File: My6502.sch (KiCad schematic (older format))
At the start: 27 parts, among them J1 IRQ_SEL, J2 CLK Jumper, J3 Barrel_Jack_Switch, J4 Expansion Port, J5 IRQ_Pullup, SW1 SW_Push_Dual, U1 28C256, U2 WD65C02, U3 CY62256-70PC, U4 74HCT00, U5 74HCT02, U6 DS1813-10, U7 74LS21, X1 CXO_DIP14

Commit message: pcb with a 10x10 board`
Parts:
- added C7: 0.1uF, Capacitor_THT:C_Disc_D4.3mm_W1.9mm_P5.00mm, symbol Device:C
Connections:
- net +5V: now also C7.1
- net GND: now also C7.2
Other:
- moved on the sheet: C6
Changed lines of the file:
@@
 L Device:C C6
 U 1 1 6163A5A8
-P 8900 4800
-F 0 "C6" H 9015 4846 50  0000 L CNN
-F 1 "0.1uF" H 9015 4755 50  0000 L CNN
-F 2 "Capacitor_THT:C_Disc_D4.3mm_W1.9mm_P5.00mm" H 8938 4650 50  0001 C CNN
-F 3 "~" H 8900 4800 50  0001 C CNN
-	1    8900 4800
+P 9050 4800
+F 0 "C6" H 9165 4846 50  0000 L CNN
+F 1 "0.1uF" H 9165 4755 50  0000 L CNN
+F 2 "Capacitor_THT:C_Disc_D4.3mm_W1.9mm_P5.00mm" H 9088 4650 50  0001 C CNN
+F 3 "~" H 9050 4800 50  0001 C CNN
+	1    9050 4800
 	1    0    0    -1
 $EndComp
@@
 	8150 5300 7700 5300
 Wire Wire Line
-	8900 4650 8900 4300
+	9050 4650 8900 4300
 Connection ~ 8900 4300
 Wire Wire Line
-	8900 4300 8150 4300
+	8900 4300 8600 4300
 Wire Wire Line
 	8150 4650 8150 4300
@@
 $EndComp
 Wire Wire Line
-	8900 5300 8150 5300
+	8900 5300 8600 5300
 Connection ~ 8900 5300
 Wire Wire Line
-	8900 4950 8900 5300
+	9050 4950 8900 5300
 Wire Wire Line
 	9500 5300 8900 5300
@@
 Wire Wire Line
 	8850 6600 8850 7450
+$Comp
+L Device:C C7
+U 1 1 63306EB2
+P 8600 4800
+F 0 "C7" H 8715 4846 50  0000 L CNN
+F 1 "0.1uF" H 8715 4755 50  0000 L CNN
+F 2 "Capacitor_THT:C_Disc_D4.3mm_W1.9mm_P5.00mm" H 8638 4650 50  0001 C CNN
+F 3 "~" H 8600 4800 50  0001 C CNN
+	1    8600 4800
+	1    0    0    -1
+$EndComp
+Wire Wire Line
+	8600 4650 8600 4300
+Connection ~ 8600 4300
+Wire Wire Line
+	8600 4300 8150 4300
+Wire Wire Line
+	8600 4950 8600 5300
+Connection ~ 8600 5300
+Wire Wire Line
+	8600 5300 8150 5300
 Wire Bus Line
 	4950 2600 4950 3800

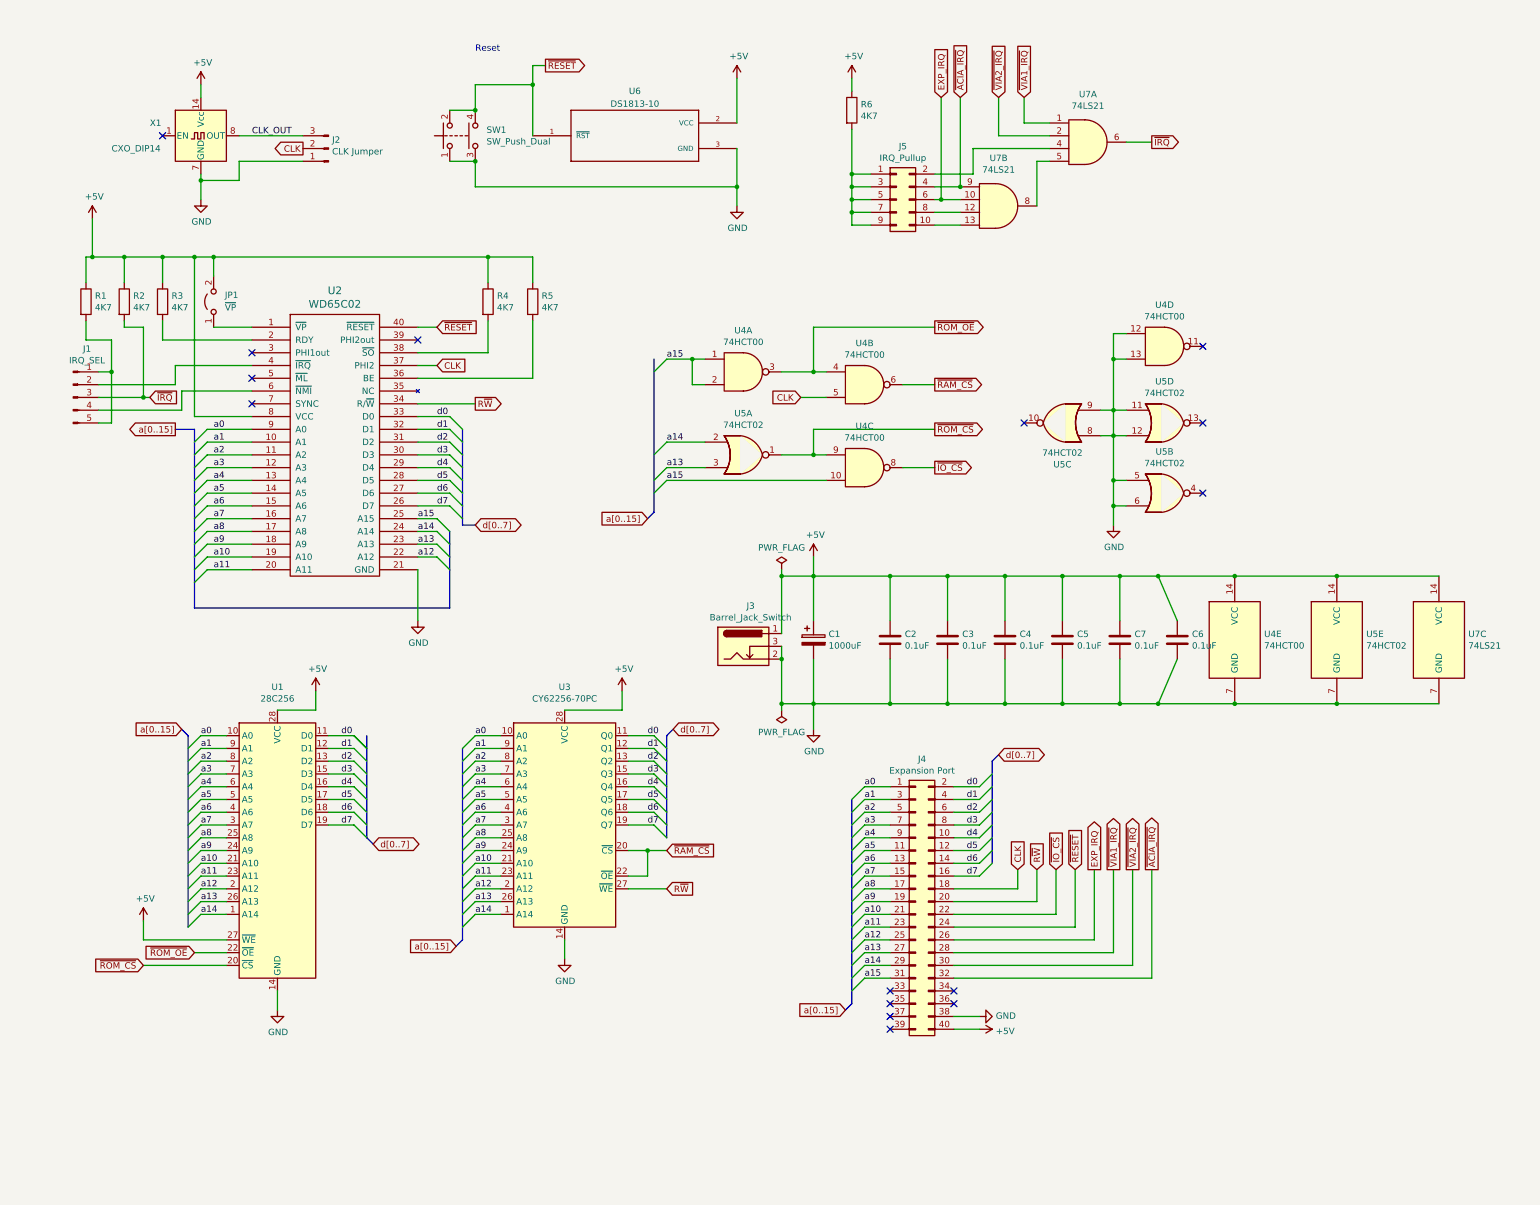
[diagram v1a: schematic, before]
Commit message: Edge board completed and routed
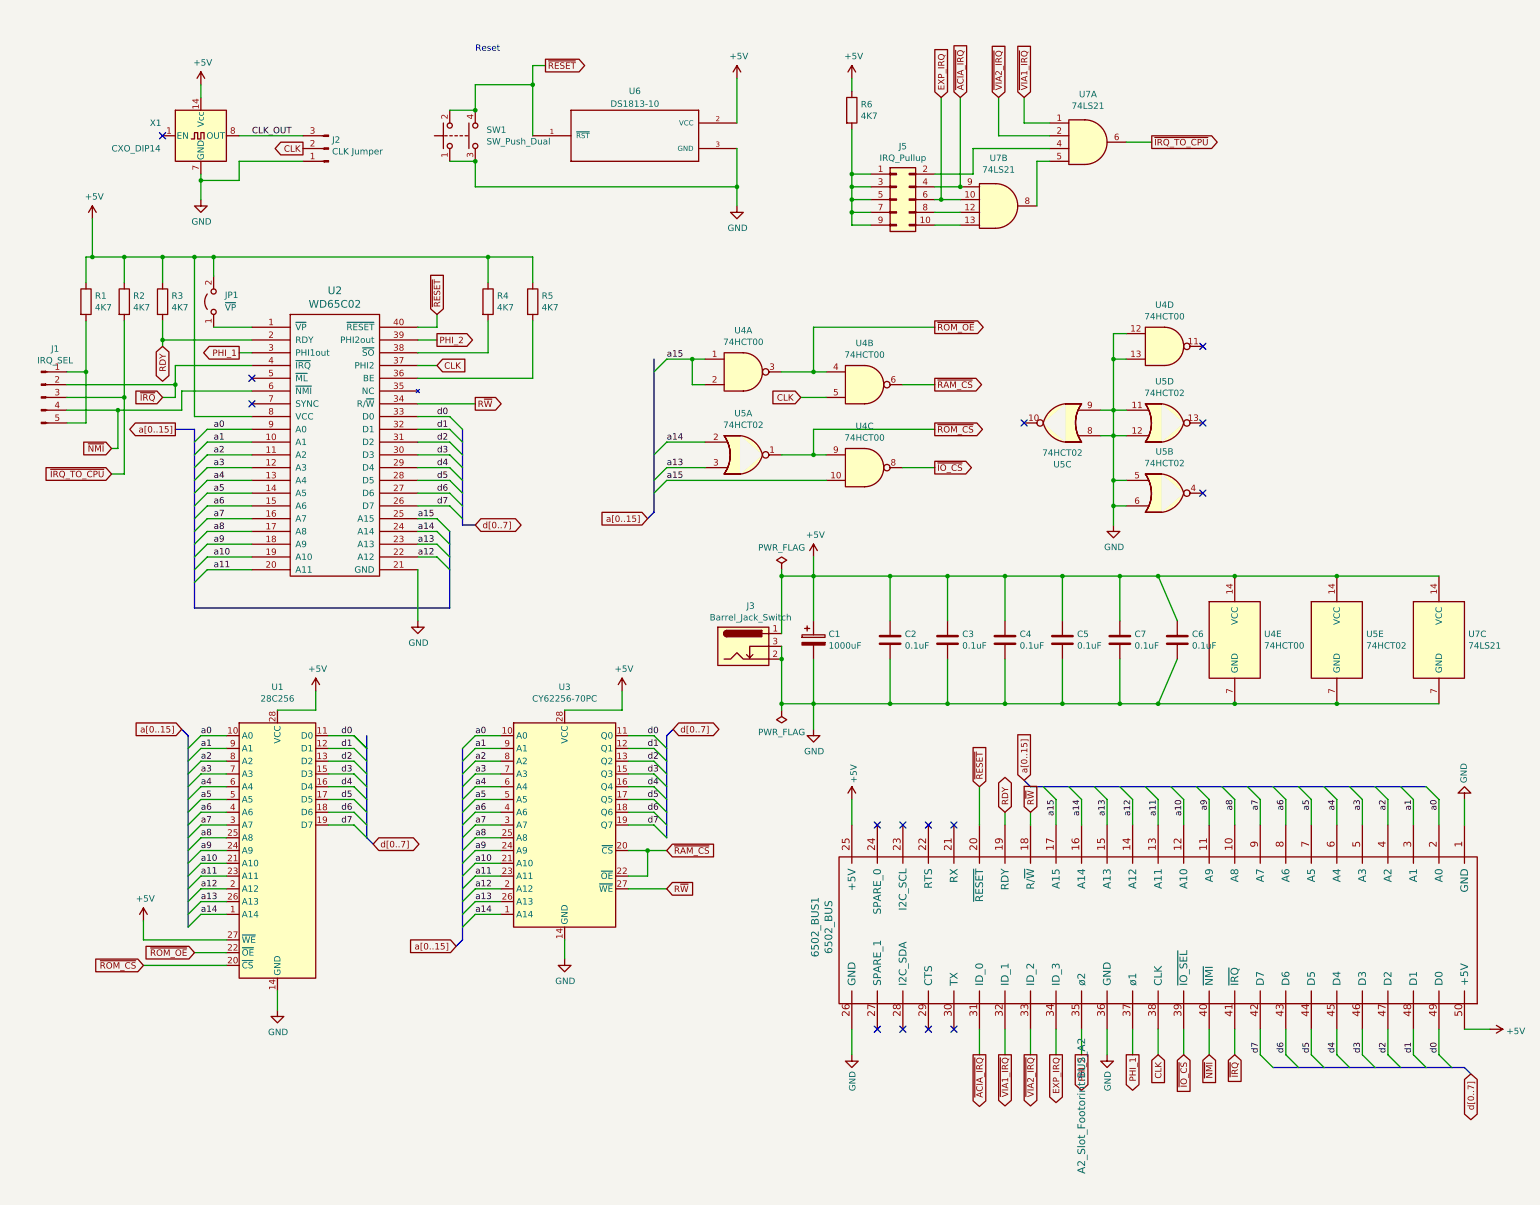
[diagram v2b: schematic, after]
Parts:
- removed J4: Expansion Port, Connector_PinSocket_2.54mm:PinSocket_2x20_P2.54mm_Vertical, symbol Connector_Generic:Conn_02x20_Odd_Even
- added 6502_BUS1: 6502_BUS, A2_Slot_Footorint:BUS_A2, symbol My6502:6502_BUS
- U2: footprint Package_DIP:DIP-40_W25.4mm_Socket_LongPads -> Package_DIP:DIP-40_W15.24mm_Socket_LongPads
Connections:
- net +5V: now also 6502_BUS1.25 (+5V), 6502_BUS1.50 (+5V)
- net CLK: now also 6502_BUS1.38 (CLK)
- net EXP_IRQ: now also 6502_BUS1.34 (ID_3)
- net GND: now also 6502_BUS1.1 (GND), 6502_BUS1.26 (GND), 6502_BUS1.36 (GND)
- net R~W: now also 6502_BUS1.18 (R/~W)
- net a0: now also 6502_BUS1.2 (A0)
- net a1: now also 6502_BUS1.3 (A1)
- net a10: now also 6502_BUS1.12 (A10)
- net a11: now also 6502_BUS1.13 (A11)
- net a12: now also 6502_BUS1.14 (A12)
- net a13: now also 6502_BUS1.15 (A13)
- net a14: now also 6502_BUS1.16 (A14)
- net a15: now also 6502_BUS1.17 (A15)
- net a2: now also 6502_BUS1.4 (A2)
- net a3: now also 6502_BUS1.5 (A3)
- net a4: now also 6502_BUS1.6 (A4)
- net a5: now also 6502_BUS1.7 (A5)
- net a6: now also 6502_BUS1.8 (A6)
- net a7: now also 6502_BUS1.9 (A7)
- net a8: now also 6502_BUS1.10 (A8)
- net a9: now also 6502_BUS1.11 (A9)
- net d0: now also 6502_BUS1.49 (D0)
- net d1: now also 6502_BUS1.48 (D1)
- net d2: now also 6502_BUS1.47 (D2)
- net d3: now also 6502_BUS1.46 (D3)
- net d4: now also 6502_BUS1.45 (D4)
- net d5: now also 6502_BUS1.44 (D5)
- net d6: now also 6502_BUS1.43 (D6)
- net d7: now also 6502_BUS1.42 (D7)
- net ~ACIA_IRQ: now also 6502_BUS1.31 (ID_0)
- net ~IO_CS: now also 6502_BUS1.39 (~IO_SEL)
- net ~IRQ: now also J1.2 (Pin_2), U2.4 (~IRQ), 6502_BUS1.41 (~IRQ); no longer J1.3 (Pin_3), R2.2, U7.6
- net ~RESET: now also 6502_BUS1.20 (~RESET)
- net ~VIA1_IRQ: now also 6502_BUS1.32 (ID_1)
- net ~VIA2_IRQ: now also 6502_BUS1.33 (ID_2)
- net RDY: now reaches R3.2, U2.2 (RDY)
- net RDY: now also 6502_BUS1.19 (RDY)
- net PHI_1: now reaches U2.3 (PHI1out)
- net PHI_1: now also 6502_BUS1.37 (ø1)
- net PHI_2: now reaches U2.39 (PHI2out)
- net PHI_2: now also 6502_BUS1.35 (ø2)
- net ~NMI: now reaches J1.4 (Pin_4), U2.6 (~NMI)
- net ~NMI: now also 6502_BUS1.40 (~NMI)
- new net ~IRQ_TO_CPU: J1.3 (Pin_3), R2.2, U7.6
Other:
- moved on the sheet: J1

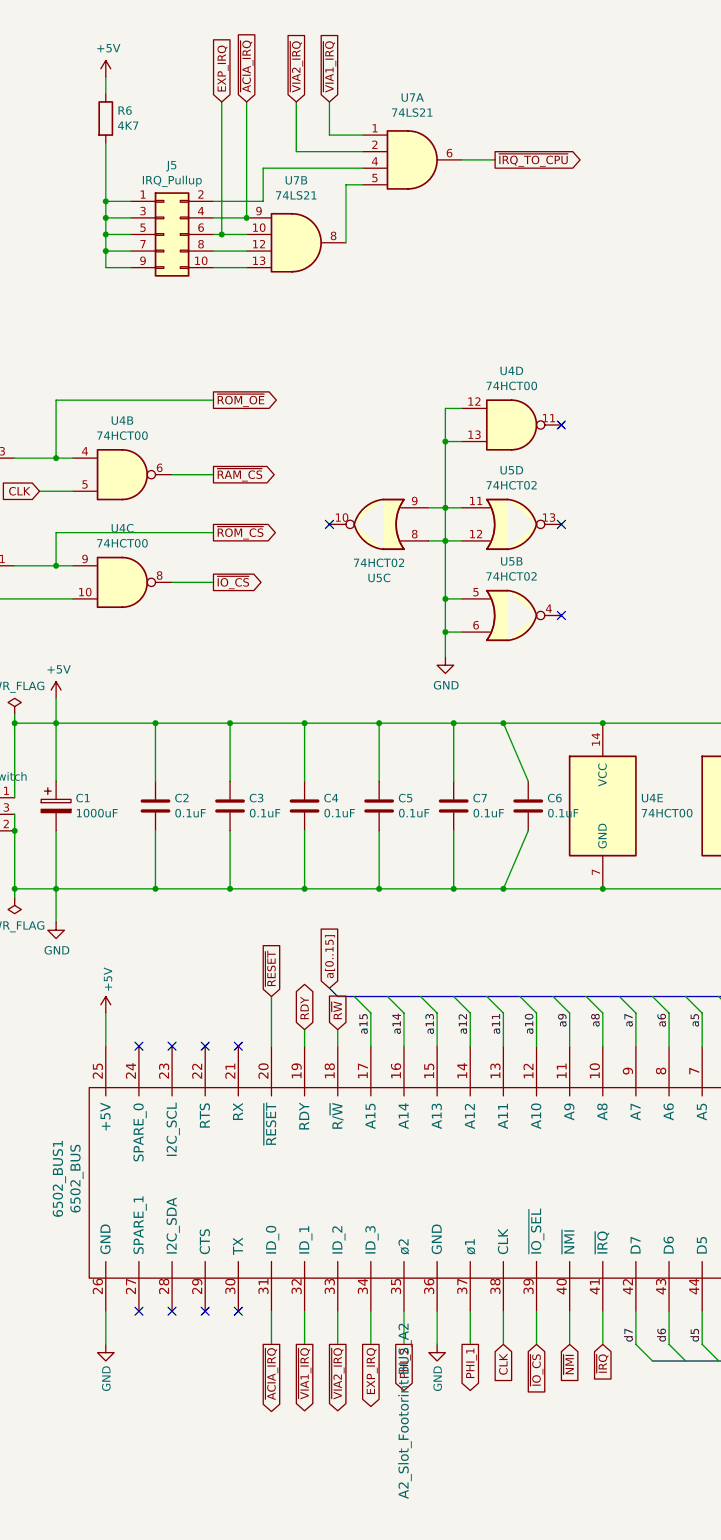
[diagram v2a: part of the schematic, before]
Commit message: moving to a backplane
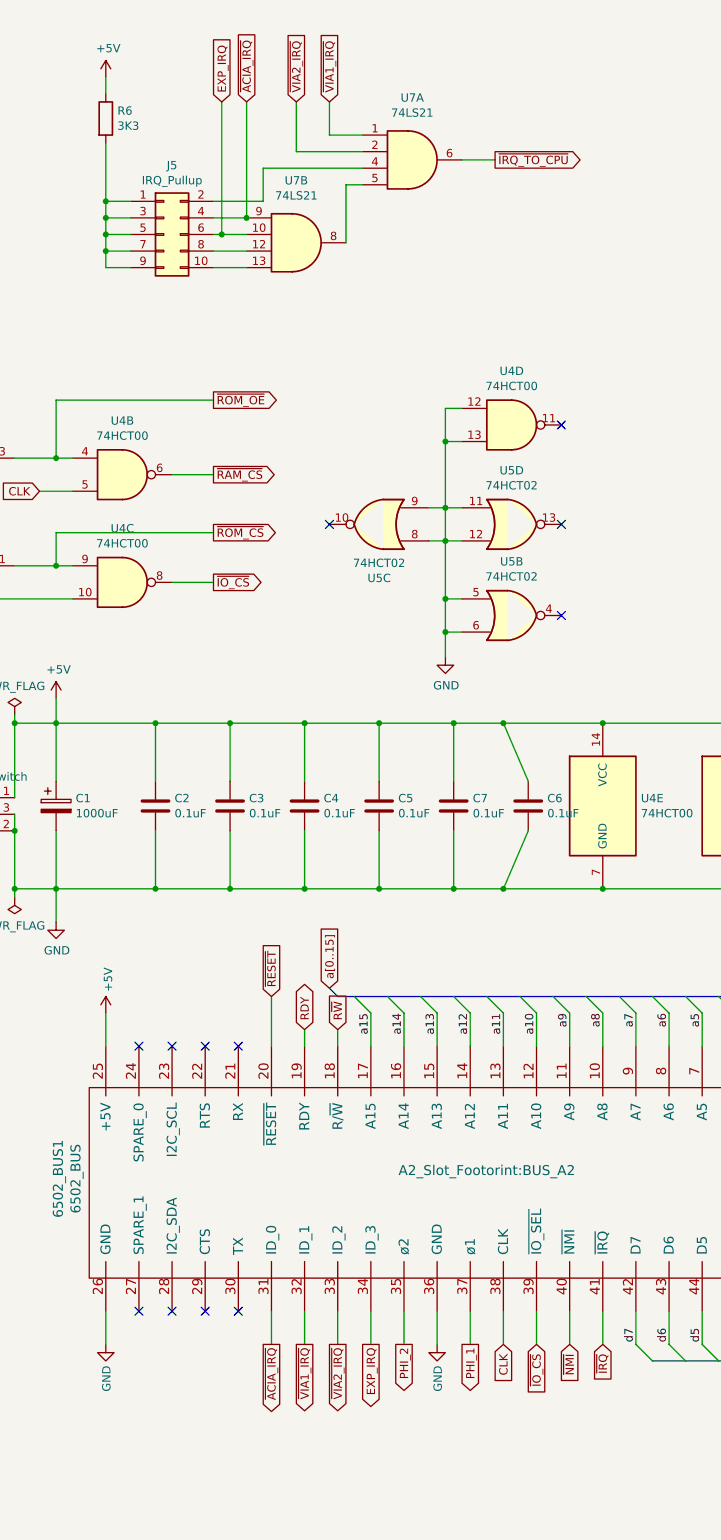
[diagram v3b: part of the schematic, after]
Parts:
- R6: value 4K7 -> 3K3
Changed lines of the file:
@@
 	800  2900 350  2900
-$Comp
-L DS1813-10:DS1813-10 U6
-U 1 1 61278A1B
-P 4800 850
-F 0 "U6" H 4800 1200 50  0000 C CNN
-F 1 "DS1813-10" H 4800 1100 50  0000 C CNN
-F 2 "Package_TO_SOT_THT:TO-92" H 4800 850 50  0001 L BNN
-F 3 "" H 4800 850 50  0001 L BNN
-F 4 "MAXIM" H 4800 850 50  0001 L BNN "VENDOR"
-F 5 "ds181315+" H 4800 850 50  0001 L BNN "MANUFACTURER_PART_NUMBER"
-	1    4800 850
-	1    0    0    -1
-$EndComp
-Text Notes 3550 200  0    50   ~ 0
-Reset
-$Comp
-L power:+5V #PWR010
-U 1 1 61279C80
-P 5600 400
-F 0 "#PWR010" H 5600 250 50  0001 C CNN
-F 1 "+5V" H 5615 573 50  0000 C CNN
-F 2 "" H 5600 400 50  0001 C CNN
-F 3 "" H 5600 400 50  0001 C CNN
-	1    5600 400
-	1    0    0    -1
-$EndComp
-$Comp
-L power:GND #PWR011
-U 1 1 6127B348
-P 5600 1400
-F 0 "#PWR011" H 5600 1150 50  0001 C CNN
-F 1 "GND" H 5605 1227 50  0000 C CNN
-F 2 "" H 5600 1400 50  0001 C CNN
-F 3 "" H 5600 1400 50  0001 C CNN
-	1    5600 1400
-	1    0    0    -1
-$EndComp
-Wire Wire Line
-	3550 1250 5600 1250
-Wire Wire Line
-	5600 1250 5600 1400
-Wire Wire Line
-	5600 950  5600 1250
-Connection ~ 5600 1250
-Wire Wire Line
-	5600 750  5600 400
 $Comp
 L Oscillator:CXO_DIP14 X1
@@
 Wire Wire Line
 	8550 2600 8550 3000
-Wire Wire Line
-	4000 850  4000 450
-Wire Wire Line
-	4000 450  3550 450
-Text GLabel 4100 300  2    50   Output ~ 0
-~RESET
 $Comp
 L Memory_RAM:CY62256-70PC U3
@@
 Wire Wire Line
 	8450 3000 8550 3000
-Connection ~ 3550 650
-Wire Wire Line
-	3550 450  3550 650
-Connection ~ 3550 1050
-Wire Wire Line
-	3550 1250 3550 1050
-Wire Wire Line
-	3350 650  3550 650
-Wire Wire Line
-	3350 1050 3550 1050
-$Comp
-L Switch:SW_Push_Dual SW1
-U 1 1 6127D438
-P 3350 850
-F 0 "SW1" V 3396 562 50  0000 R CNN
-F 1 "SW_Push_Dual" V 3305 562 50  0000 R CNN
-F 2 "Button_Switch_THT:SW_TH_Tactile_Omron_B3F-10xx" H 3350 1050 50  0001 C CNN
-F 3 "~" H 3350 1050 50  0001 C CNN
-	1    3350 850
-	0    -1   -1   0
-$EndComp
-Wire Wire Line
-	4100 300  4000 300
-Wire Wire Line
-	4000 300  4000 450
-Connection ~ 4000 450
 $Comp
 L 74xx:74LS21 U7
@@
 P 6500 650
 F 0 "R6" H 6570 696 50  0000 L CNN
-F 1 "4K7" H 6570 605 50  0000 L CNN
+F 1 "3K3" H 6570 605 50  0000 L CNN
 F 2 "Resistor_THT:R_Axial_DIN0207_L6.3mm_D2.5mm_P10.16mm_Horizontal" V 6430 650 50  0001 L CNN
 F 3 "~" H 6500 650 50  0001 L CNN
@@
 F 0 "6502_BUS1" H 9700 10537 60  0000 C CNN
 F 1 "6502_BUS" H 9700 10431 60  0000 C CNN
-F 2 "A2_Slot_Footorint:BUS_A2" H 8300 8450 60  0000 C CNN
+F 2 "A2_Slot_Footorint:BUS_A2" V 9750 7950 60  0000 C CNN
 F 3 "" H 8300 8450 60  0000 C CNN
 	1    8300 8450
@@
 	8100 8050 8100 7850
 Wire Bus Line
+	9800 8150 11300 8150
+Wire Bus Line
+	7900 5950 11000 5950
+Wire Bus Line
+	1300 5550 1300 7050
+Wire Bus Line
+	3450 5650 3450 7150
+Wire Bus Line
+	5050 5550 5050 6350
+Wire Bus Line
+	2700 5550 2700 6350
+Wire Bus Line
 	4950 2600 4950 3800
 Wire Bus Line
+	1350 3150 1350 4550
+Wire Bus Line
 	3350 3950 3350 4550
 Wire Bus Line
-	9800 8150 11300 8150
-Wire Bus Line
-	5050 5550 5050 6350
-Wire Bus Line
-	2700 5550 2700 6350
-Wire Bus Line
 	3450 3150 3450 3900
-Wire Bus Line
-	1350 3150 1350 4550
-Wire Bus Line
-	3450 5650 3450 7150
-Wire Bus Line
-	1300 5550 1300 7050
-Wire Bus Line
-	7900 5950 11000 5950
+Connection ~ 4000 450
+Wire Wire Line
+	4000 300  4000 450
+Wire Wire Line
+	4100 300  4000 300
+$Comp
+L Switch:SW_Push_Dual SW1
+U 1 1 6127D438
+P 3350 850
+F 0 "SW1" V 3396 562 50  0000 R CNN
+F 1 "SW_Push_Dual" V 3305 562 50  0000 R CNN
+F 2 "Button_Switch_THT:SW_TH_Tactile_Omron_B3F-10xx" H 3350 1050 50  0001 C CNN
+F 3 "~" H 3350 1050 50  0001 C CNN
+	1    3350 850
+	0    -1   -1   0
+$EndComp
+Wire Wire Line
+	3350 1050 3550 1050
+Wire Wire Line
+	3350 650  3550 650
+Wire Wire Line
+	3550 1250 3550 1050
+Connection ~ 3550 1050
+Wire Wire Line
+	3550 450  3550 650
+Connection ~ 3550 650
+Text GLabel 4100 300  2    50   Output ~ 0
+~RESET
+Wire Wire Line
+	4000 450  3550 450
+Wire Wire Line
+	4000 850  4000 450
+Wire Wire Line
+	5600 750  5600 400
+Connection ~ 5600 1250
+Wire Wire Line
+	5600 950  5600 1250
+Wire Wire Line
+	5600 1250 5600 1400
+Wire Wire Line
+	3550 1250 5600 1250
+$Comp
+L power:GND #PWR011
+U 1 1 6127B348
+P 5600 1400
+F 0 "#PWR011" H 5600 1150 50  0001 C CNN
+F 1 "GND" H 5605 1227 50  0000 C CNN
+F 2 "" H 5600 1400 50  0001 C CNN
+F 3 "" H 5600 1400 50  0001 C CNN
+	1    5600 1400
+	1    0    0    -1
+$EndComp
+$Comp
+L power:+5V #PWR010
+U 1 1 61279C80
+P 5600 400
+F 0 "#PWR010" H 5600 250 50  0001 C CNN
+F 1 "+5V" H 5615 573 50  0000 C CNN
+F 2 "" H 5600 400 50  0001 C CNN
+F 3 "" H 5600 400 50  0001 C CNN
+	1    5600 400
+	1    0    0    -1
+$EndComp
+Text Notes 3550 200  0    50   ~ 0
+Reset
+$Comp
+L DS1813-10:DS1813-10 U6
+U 1 1 61278A1B
+P 4800 850
+F 0 "U6" H 4800 1200 50  0000 C CNN
+F 1 "DS1813-10" H 4800 1100 50  0000 C CNN
+F 2 "Package_TO_SOT_THT:TO-92" H 4800 850 50  0001 L BNN
+F 3 "" H 4800 850 50  0001 L BNN
+F 4 "MAXIM" H 4800 850 50  0001 L BNN "VENDOR"
+F 5 "ds181315+" H 4800 850 50  0001 L BNN "MANUFACTURER_PART_NUMBER"
+	1    4800 850
+	1    0    0    -1
+$EndComp
 $EndSCHEMATC
